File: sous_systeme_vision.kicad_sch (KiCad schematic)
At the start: 10 parts, among them M18 Fan, 5V, M19 Fan, 5V, U29 Arducam_OV2311_Global_Shutter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, U31 Orange_Pi_5, U32 Arducam_OV2311_Global_Shutter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, U34 Orange_Pi_5

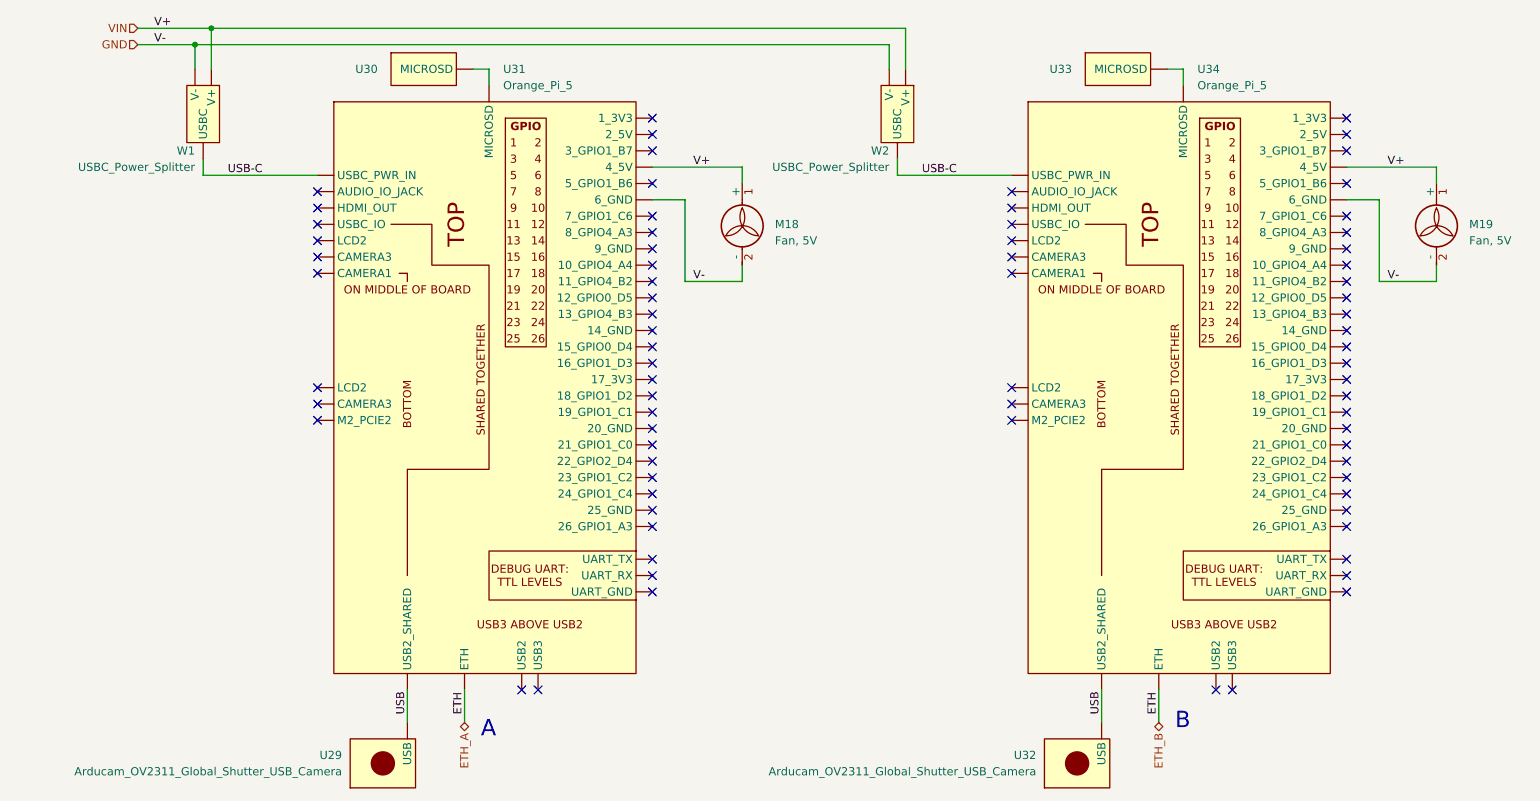
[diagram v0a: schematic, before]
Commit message: Ajout Limelight + webcam
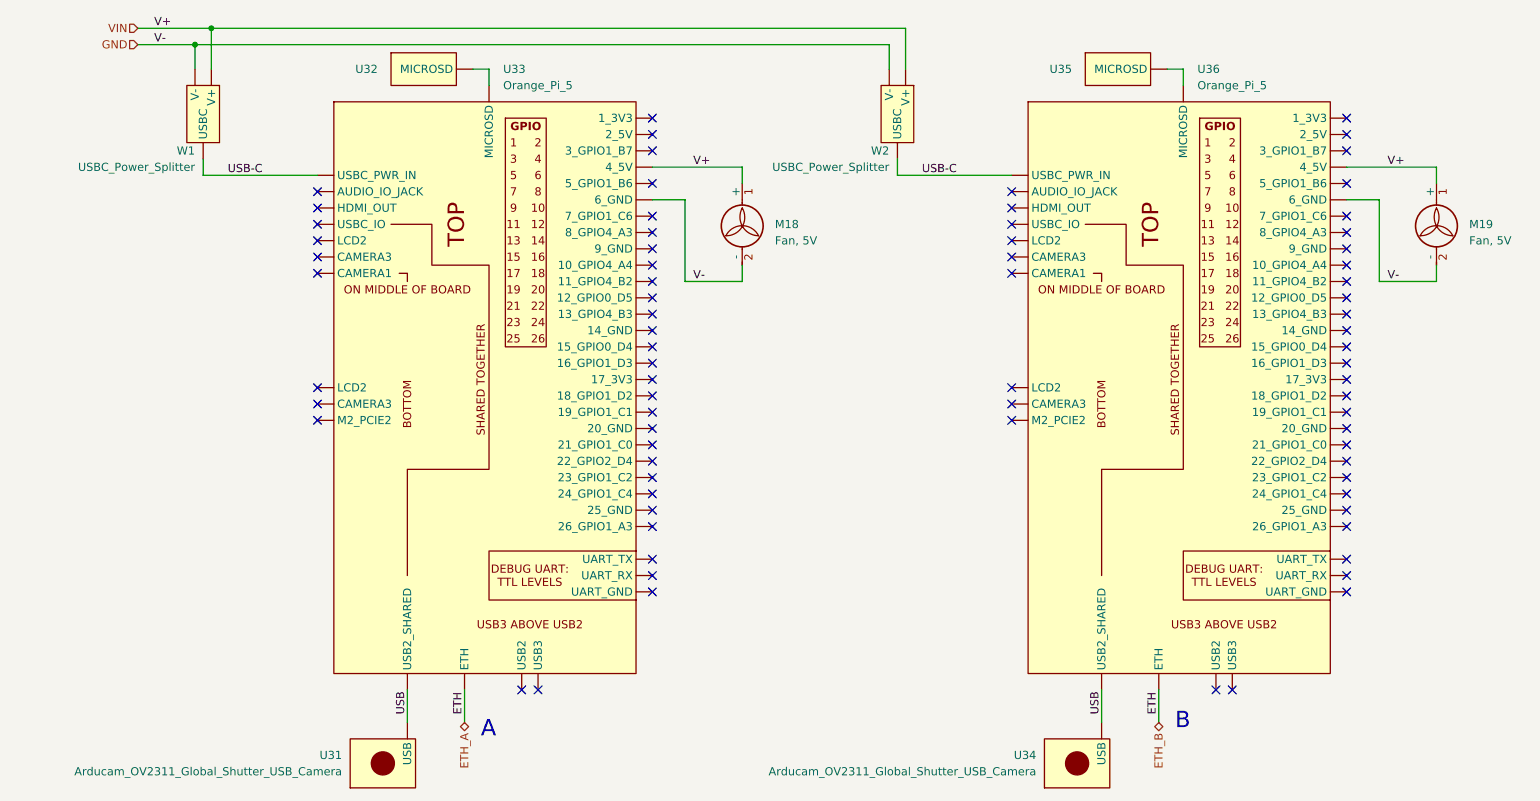
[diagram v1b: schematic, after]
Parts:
- renumbered U29 to U31, U30 to U32, U31 to U33, U32 to U34, U33 to U35, U34 to U36
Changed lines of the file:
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@@
   (title_block
     (title "Schéma de câblage Disc-O 2024")
-    (date "2024-02-17")
-    (rev "1.5")
+    (date "2024-02-27")
+    (rev "1.6")
     (company "ASTRO 7605 (2024)")
   )
@@
   (symbol (lib_id "FRC_Components:Arducam_OV2311_Global_Shutter_USB_Camera") (at 173.99 139.7 0) (mirror x) (unit 1)
     (in_bom yes) (on_board yes) (dnp no)
-    (property "Reference" "U32" (at 167.64 128.27 0)
+    (property "Reference" "U34" (at 167.64 128.27 0)
       (effects (font (size 1.27 1.27)) (justify right))
     )
@@
       (project "schema_cablage_2024"
         (path "/e63e39d7-6ac0-4ffd-8aa3-1841a4541b55/1b3a1c37-25c1-4c56-8214-aa5c607a7a96"
-          (reference "U32") (unit 1)
+          (reference "U34") (unit 1)
         )
       )
@@
   (symbol (lib_id "FRC_Components:MicroSD_Card") (at 72.39 17.78 0) (unit 1)
     (in_bom yes) (on_board yes) (dnp no)
-    (property "Reference" "U30" (at 63.5 21.59 0)
+    (property "Reference" "U32" (at 63.5 21.59 0)
       (effects (font (size 1.27 1.27)))
     )
@@
       (project "schema_cablage_2024"
         (path "/e63e39d7-6ac0-4ffd-8aa3-1841a4541b55/1b3a1c37-25c1-4c56-8214-aa5c607a7a96"
-          (reference "U30") (unit 1)
+          (reference "U32") (unit 1)
         )
       )
@@
   (symbol (lib_id "FRC_Components:Orange_Pi_5") (at 82.55 12.7 0) (unit 1)
     (in_bom yes) (on_board yes) (dnp no) (fields_autoplaced)
-    (property "Reference" "U31" (at 84.7441 21.59 0)
+    (property "Reference" "U33" (at 84.7441 21.59 0)
       (effects (font (size 1.27 1.27)) (justify left))
     )
@@
       (project "schema_cablage_2024"
         (path "/e63e39d7-6ac0-4ffd-8aa3-1841a4541b55/1b3a1c37-25c1-4c56-8214-aa5c607a7a96"
-          (reference "U31") (unit 1)
+          (reference "U33") (unit 1)
         )
       )
@@
   (symbol (lib_id "FRC_Components:Orange_Pi_5") (at 190.5 12.7 0) (unit 1)
     (in_bom yes) (on_board yes) (dnp no) (fields_autoplaced)
-    (property "Reference" "U34" (at 192.6941 21.59 0)
+    (property "Reference" "U36" (at 192.6941 21.59 0)
       (effects (font (size 1.27 1.27)) (justify left))
     )
@@
       (project "schema_cablage_2024"
         (path "/e63e39d7-6ac0-4ffd-8aa3-1841a4541b55/1b3a1c37-25c1-4c56-8214-aa5c607a7a96"
-          (reference "U34") (unit 1)
+          (reference "U36") (unit 1)
         )
       )
@@
   (symbol (lib_id "FRC_Components:MicroSD_Card") (at 180.34 17.78 0) (unit 1)
     (in_bom yes) (on_board yes) (dnp no)
-    (property "Reference" "U33" (at 171.45 21.59 0)
+    (property "Reference" "U35" (at 171.45 21.59 0)
       (effects (font (size 1.27 1.27)))
     )
@@
       (project "schema_cablage_2024"
         (path "/e63e39d7-6ac0-4ffd-8aa3-1841a4541b55/1b3a1c37-25c1-4c56-8214-aa5c607a7a96"
-          (reference "U33") (unit 1)
+          (reference "U35") (unit 1)
         )
       )
@@
   (symbol (lib_id "FRC_Components:Arducam_OV2311_Global_Shutter_USB_Camera") (at 66.04 139.7 0) (mirror x) (unit 1)
     (in_bom yes) (on_board yes) (dnp no)
-    (property "Reference" "U29" (at 59.69 128.27 0)
+    (property "Reference" "U31" (at 59.69 128.27 0)
       (effects (font (size 1.27 1.27)) (justify right))
     )
@@
       (project "schema_cablage_2024"
         (path "/e63e39d7-6ac0-4ffd-8aa3-1841a4541b55/1b3a1c37-25c1-4c56-8214-aa5c607a7a96"
-          (reference "U29") (unit 1)
-        )
-      )
+          (reference "U31") (unit 1)
+        )
+      )
